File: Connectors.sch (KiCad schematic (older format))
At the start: 12 parts, among them J10 JST-PH, J11 USB_C_Receptacle_USB2.0, J9 Micro_SD_Card_Det, U8 USBLC6-2SC6

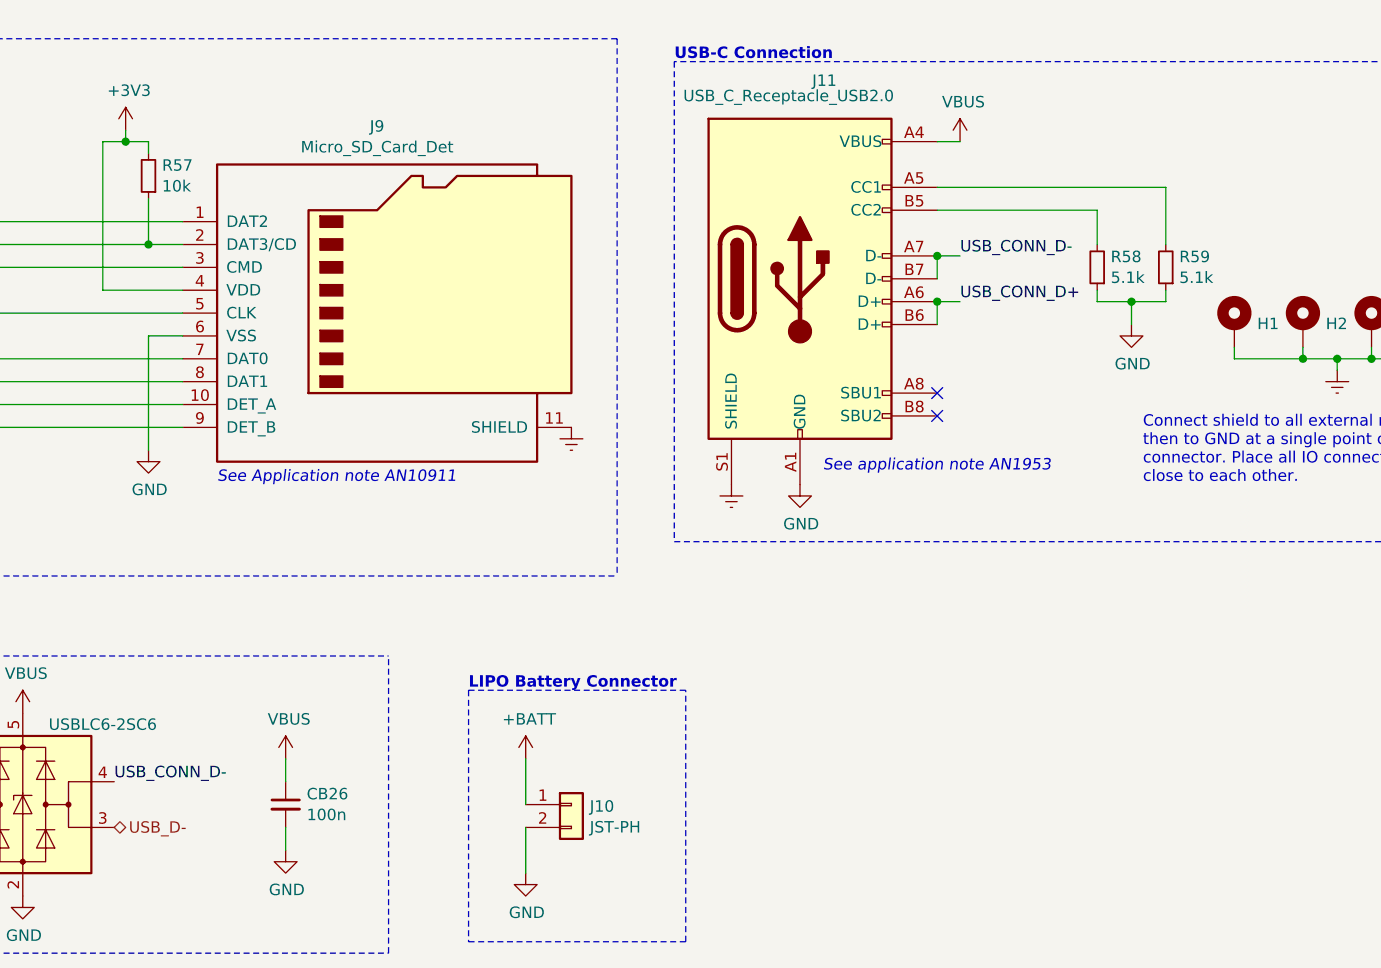
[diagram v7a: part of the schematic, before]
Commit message: Change Mic Preamp
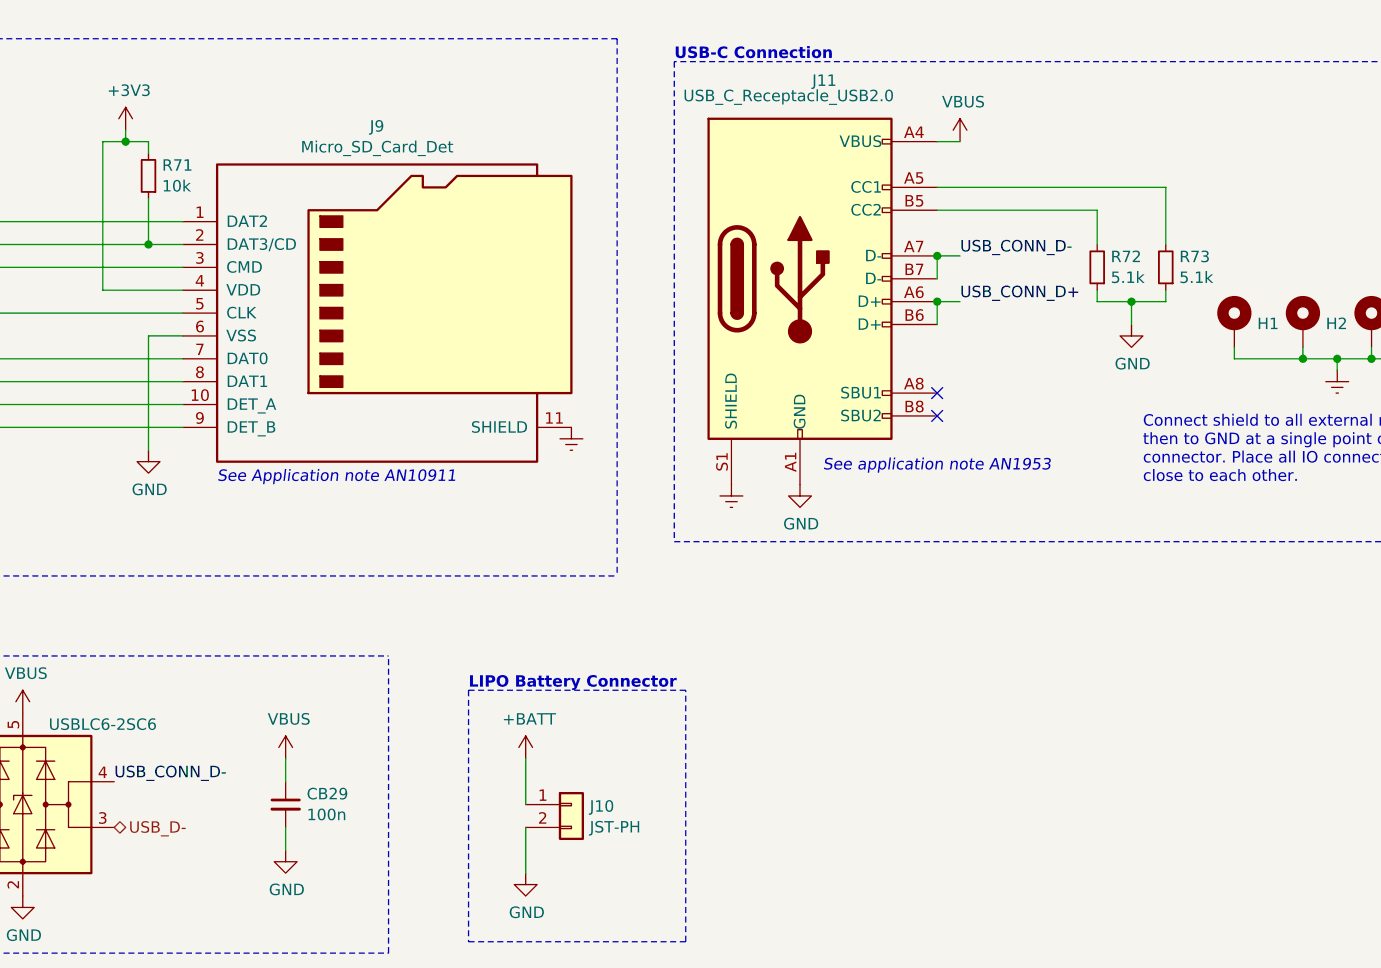
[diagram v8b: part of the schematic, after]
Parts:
- CB29: renamed from CB26; MPN (none) -> C0603C104M5RACTU; Mfr. (none) -> KEMET
- R72: renamed from R58; MPN (none) -> AC0603FR-135K1L; Mfr. (none) -> Yageo
- R73: renamed from R59; MPN (none) -> AC0603FR-135K1L; Mfr. (none) -> Yageo
- renumbered R57 to R71
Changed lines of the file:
@@
 $EndDescr
 $Comp
-L power:GND #PWR0116
+L power:GND #PWR0124
 U 1 1 5EF579E9
 P 7200 4000
-F 0 "#PWR0116" H 7200 3750 50  0001 C CNN
+F 0 "#PWR0124" H 7200 3750 50  0001 C CNN
 F 1 "GND" H 7205 3827 50  0000 C CNN
 F 2 "" H 7200 4000 50  0001 C CNN
@@
 $EndComp
 $Comp
-L power:Earth #PWR0115
+L power:Earth #PWR0123
 U 1 1 5EF579EF
 P 6900 4000
-F 0 "#PWR0115" H 6900 3750 50  0001 C CNN
+F 0 "#PWR0123" H 6900 3750 50  0001 C CNN
 F 1 "Earth" H 6900 3850 50  0001 C CNN
 F 2 "" H 6900 4000 50  0001 C CNN
@@
 $EndComp
 $Comp
-L power:VBUS #PWR0117
+L power:VBUS #PWR0125
 U 1 1 5EF579F5
 P 7900 2500
-F 0 "#PWR0117" H 7900 2350 50  0001 C CNN
+F 0 "#PWR0125" H 7900 2350 50  0001 C CNN
 F 1 "VBUS" H 7915 2673 50  0000 C CNN
 F 2 "" H 7900 2500 50  0001 C CNN
@@
 NoConn ~ 7800 3600
 $Comp
-L Device:R_Small R58
+L Device:R_Small R72
 U 1 1 5EF57A0A
 P 8500 3050
-F 0 "R58" H 8441 3004 50  0000 R CNN
+F 0 "R72" H 8441 3004 50  0000 R CNN
 F 1 "5.1k" H 8441 3095 50  0000 R CNN
 F 2 "Resistor_SMD:R_0603_1608Metric_Pad1.05x0.95mm_HandSolder" H 8500 3050 50  0001 C CNN
 F 3 "~" H 8500 3050 50  0001 C CNN
+F 4 "AC0603FR-135K1L" H 8500 3050 50  0001 C CNN "MPN"
+F 5 "Yageo" H 8500 3050 50  0001 C CNN "Mfr."
 	1    8500 3050
 	-1   0    0    1
 $EndComp
 $Comp
-L Device:R_Small R59
+L Device:R_Small R73
 U 1 1 5EF57A10
 P 8800 3050
-F 0 "R59" H 8741 3004 50  0000 R CNN
+F 0 "R73" H 8741 3004 50  0000 R CNN
 F 1 "5.1k" H 8741 3095 50  0000 R CNN
 F 2 "Resistor_SMD:R_0603_1608Metric_Pad1.05x0.95mm_HandSolder" H 8800 3050 50  0001 C CNN
 F 3 "~" H 8800 3050 50  0001 C CNN
+F 4 "AC0603FR-135K1L" H 8800 3050 50  0001 C CNN "MPN"
+F 5 "Yageo" H 8800 3050 50  0001 C CNN "Mfr."
 	1    8800 3050
 	-1   0    0    1
@@
 	8800 2700 7800 2700
 $Comp
-L power:GND #PWR0118
+L power:GND #PWR0126
 U 1 1 5EF57A1A
 P 8650 3300
-F 0 "#PWR0118" H 8650 3050 50  0001 C CNN
+F 0 "#PWR0126" H 8650 3050 50  0001 C CNN
 F 1 "GND" H 8655 3127 50  0000 C CNN
 F 2 "" H 8650 3300 50  0001 C CNN
@@
 	9550 3500 9550 3450
 $Comp
-L power:Earth #PWR0119
+L power:Earth #PWR0127
 U 1 1 5EF57A38
 P 9550 3500
-F 0 "#PWR0119" H 9550 3250 50  0001 C CNN
+F 0 "#PWR0127" H 9550 3250 50  0001 C CNN
 F 1 "Earth" H 9550 3350 50  0001 C CNN
 F 2 "" H 9550 3500 50  0001 C CNN
@@
 USB-C Connection
 $Comp
-L power:Earth #PWR0114
+L power:Earth #PWR0122
 U 1 1 5EF59730
 P 6200 3750
-F 0 "#PWR0114" H 6200 3500 50  0001 C CNN
+F 0 "#PWR0122" H 6200 3500 50  0001 C CNN
 F 1 "Earth" H 6200 3600 50  0001 C CNN
 F 2 "" H 6200 3750 50  0001 C CNN
@@
 SDIO_WP
 $Comp
-L power:GND #PWR0109
+L power:GND #PWR0117
 U 1 1 5EFBCDAD
 P 4350 3850
-F 0 "#PWR0109" H 4350 3600 50  0001 C CNN
+F 0 "#PWR0117" H 4350 3600 50  0001 C CNN
 F 1 "GND" H 4355 3677 50  0000 C CNN
 F 2 "" H 4350 3850 50  0001 C CNN
@@
 $EndComp
 $Comp
-L power:+BATT #PWR0112
+L power:+BATT #PWR0120
 U 1 1 5EE0C94B
 P 6000 5200
-F 0 "#PWR0112" H 6000 5050 50  0001 C CNN
+F 0 "#PWR0120" H 6000 5050 50  0001 C CNN
 F 1 "+BATT" H 6015 5373 50  0000 C CNN
 F 2 "" H 6000 5200 50  0001 C CNN
@@
 $EndComp
 $Comp
-L power:GND #PWR0113
+L power:GND #PWR0121
 U 1 1 5EE0C951
 P 6000 5700
-F 0 "#PWR0113" H 6000 5450 50  0001 C CNN
+F 0 "#PWR0121" H 6000 5450 50  0001 C CNN
 F 1 "GND" H 6005 5527 50  0000 C CNN
 F 2 "" H 6000 5700 50  0001 C CNN
@@
 $EndComp
 $Comp
-L power:GND #PWR0107
+L power:GND #PWR0115
 U 1 1 5EF9E21E
 P 3800 5800
-F 0 "#PWR0107" H 3800 5550 50  0001 C CNN
+F 0 "#PWR0115" H 3800 5550 50  0001 C CNN
 F 1 "GND" H 3805 5627 50  0000 C CNN
 F 2 "" H 3800 5800 50  0001 C CNN
@@
 $EndComp
 $Comp
-L power:VBUS #PWR0106
+L power:VBUS #PWR0114
 U 1 1 5EF9EE8C
 P 3800 5000
-F 0 "#PWR0106" H 3800 4850 50  0001 C CNN
+F 0 "#PWR0114" H 3800 4850 50  0001 C CNN
 F 1 "VBUS" H 3815 5173 50  0000 C CNN
 F 2 "" H 3800 5000 50  0001 C CNN
@@
 USB ESD Protection
 $Comp
-L Device:C_Small CB26
+L Device:C_Small CB29
 U 1 1 5EFBCA6D
 P 4950 5400
-F 0 "CB26" H 5042 5446 50  0000 L CNN
+F 0 "CB29" H 5042 5446 50  0000 L CNN
 F 1 "100n" H 5042 5355 50  0000 L CNN
 F 2 "Capacitor_SMD:C_0603_1608Metric_Pad1.05x0.95mm_HandSolder" H 4950 5400 50  0001 C CNN
 F 3 "~" H 4950 5400 50  0001 C CNN
+F 4 "C0603C104M5RACTU" H 4950 5400 50  0001 C CNN "MPN"
+F 5 "KEMET" H 4950 5400 50  0001 C CNN "Mfr."
 	1    4950 5400
 	1    0    0    -1
 $EndComp
 $Comp
-L power:VBUS #PWR0110
+L power:VBUS #PWR0118
 U 1 1 5EFBD2C9
 P 4950 5200
-F 0 "#PWR0110" H 4950 5050 50  0001 C CNN
+F 0 "#PWR0118" H 4950 5050 50  0001 C CNN
 F 1 "VBUS" H 4965 5373 50  0000 C CNN
 F 2 "" H 4950 5200 50  0001 C CNN
@@
 $EndComp
 $Comp
-L power:GND #PWR0111
+L power:GND #PWR0119
 U 1 1 5EFBD729
 P 4950 5600
-F 0 "#PWR0111" H 4950 5350 50  0001 C CNN
+F 0 "#PWR0119" H 4950 5350 50  0001 C CNN
 F 1 "GND" H 4955 5427 50  0000 C CNN
 F 2 "" H 4950 5600 50  0001 C CNN
@@
 	2750 4750 5400 4750
 $Comp
-L Device:R_Small R57
+L Device:R_Small R71
 U 1 1 5EF7DC5F
 P 4350 2650
-F 0 "R57" H 4291 2604 50  0000 R CNN
+F 0 "R71" H 4291 2604 50  0000 R CNN
 F 1 "10k" H 4291 2695 50  0000 R CNN
 F 2 "Resistor_SMD:R_0603_1608Metric_Pad1.05x0.95mm_HandSolder" H 4350 2650 50  0001 C CNN
@@
 $EndComp
 $Comp
-L power:+3V3 #PWR0108
+L power:+3V3 #PWR0116
 U 1 1 5EF922F3
 P 4250 2450
-F 0 "#PWR0108" H 4250 2300 50  0001 C CNN
+F 0 "#PWR0116" H 4250 2300 50  0001 C CNN
 F 1 "+3V3" H 4265 2623 50  0000 C CNN
 F 2 "" H 4250 2450 50  0001 C CNN
